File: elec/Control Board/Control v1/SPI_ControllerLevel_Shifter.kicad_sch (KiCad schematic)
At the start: 34 parts, among them J301 RJ12_6P6C_HORZ, J302 0.100_2Pin, Q301 BSS138, Q302 BSS138, Q303 BSS138, Q304 BSS138

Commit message: Update parts in schematic for BOM generation.
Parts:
- R308, R313, R316, R317: MPN RMC 0603 10K F N -> RMC060310KFN
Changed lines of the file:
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@@
       (effects (font (size 1.27 1.27)) hide)
     )
-    (property "Description" "100mW ±1% 1kΩ 0603 Chip Resistor" (at 120.65 83.82 0)
+    (property "Description" "0.1W ±1% 1kΩ 0603 Chip Resistor - Surface Mount ROHS" (at 120.65 83.82 0)
       (effects (font (size 1.27 1.27)) hide)
     )
@@
       (effects (font (size 1.27 1.27)) hide)
     )
-    (property "Datasheet" "~" (at 143.51 138.43 0)
+    (property "Datasheet" "https://datasheet.lcsc.com/lcsc/1811101310_TyoHM-RMC06031K1-N_C269704.pdf" (at 143.51 138.43 0)
       (effects (font (size 1.27 1.27)) hide)
     )
@@
       (effects (font (size 1.27 1.27)) hide)
     )
-    (property "MPN" "RMC 0603 10K F N" (at 143.51 138.43 0)
+    (property "MPN" "RMC060310KFN" (at 143.51 138.43 0)
       (effects (font (size 1.27 1.27)) hide)
     )
@@
       (effects (font (size 1.27 1.27)) hide)
     )
-    (property "Datasheet" "~" (at 142.24 176.53 0)
+    (property "Datasheet" "https://datasheet.lcsc.com/lcsc/1811101310_TyoHM-RMC06031K1-N_C269704.pdf" (at 142.24 176.53 0)
       (effects (font (size 1.27 1.27)) hide)
     )
@@
       (effects (font (size 1.27 1.27)) hide)
     )
-    (property "MPN" "RMC 0603 10K F N" (at 142.24 176.53 0)
+    (property "MPN" "RMC060310KFN" (at 142.24 176.53 0)
       (effects (font (size 1.27 1.27)) hide)
     )
@@
       (effects (font (size 1.27 1.27)) hide)
     )
-    (property "Datasheet" "~" (at 143.51 101.6 0)
+    (property "Datasheet" "https://datasheet.lcsc.com/lcsc/1811101310_TyoHM-RMC06031K1-N_C269704.pdf" (at 143.51 101.6 0)
       (effects (font (size 1.27 1.27)) hide)
     )
@@
       (effects (font (size 1.27 1.27)) hide)
     )
-    (property "MPN" "RMC 0603 10K F N" (at 143.51 101.6 0)
+    (property "MPN" "RMC060310KFN" (at 143.51 101.6 0)
       (effects (font (size 1.27 1.27)) hide)
     )
@@
       (effects (font (size 1.27 1.27)) hide)
     )
-    (property "Description" "100mW ±1% 1kΩ 0603 Chip Resistor" (at 119.38 158.75 0)
+    (property "Description" "0.1W ±1% 1kΩ 0603 Chip Resistor - Surface Mount ROHS" (at 119.38 158.75 0)
       (effects (font (size 1.27 1.27)) hide)
     )
@@
       (effects (font (size 1.27 1.27)) hide)
     )
-    (property "Datasheet" "~" (at 120.65 49.53 0)
+    (property "Datasheet" "https://datasheet.lcsc.com/lcsc/1811101310_TyoHM-RMC06031K1-N_C269704.pdf" (at 120.65 49.53 0)
       (effects (font (size 1.27 1.27)) hide)
     )
@@
       (effects (font (size 1.27 1.27)) hide)
     )
-    (property "MPN" "RMC 0603 10K F N" (at 120.65 49.53 0)
+    (property "MPN" "RMC060310KFN" (at 120.65 49.53 0)
       (effects (font (size 1.27 1.27)) hide)
     )
@@
       (effects (font (size 1.27 1.27)) hide)
     )
-    (property "Description" "100mW ±1% 1kΩ 0603 Chip Resistor" (at 120.65 120.65 0)
+    (property "Description" "0.1W ±1% 1kΩ 0603 Chip Resistor - Surface Mount ROHS" (at 120.65 120.65 0)
       (effects (font (size 1.27 1.27)) hide)
     )
@@
       (effects (font (size 1.27 1.27)) hide)
     )
-    (property "Description" "100mW ±1% 1kΩ 0603 Chip Resistor" (at 143.51 67.31 0)
-      (effects (font (size 1.27 1.27)) hide)
-    )
+    (property "Description" "0.1W ±1% 1kΩ 0603 Chip Resistor - Surface Mount ROHS" (at 143.51 67.31 0)
+      (effects (font (size 1.27 1.27)) hide)
+    )

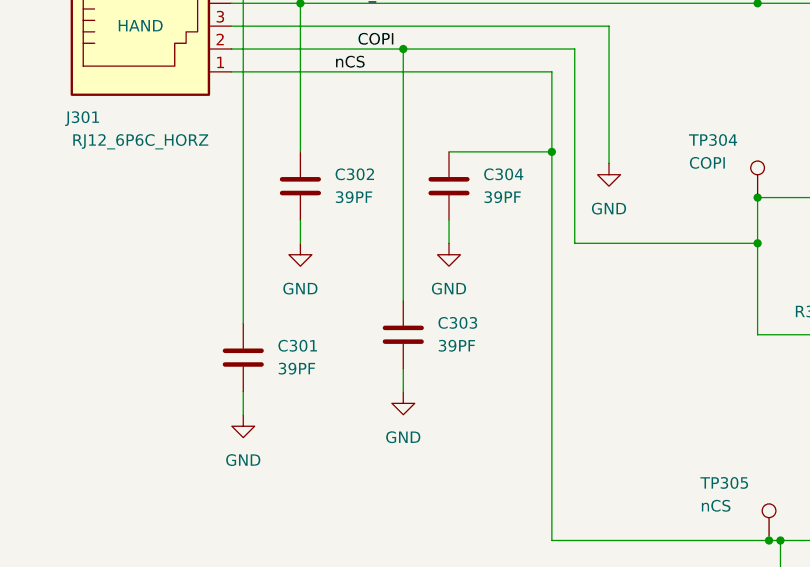
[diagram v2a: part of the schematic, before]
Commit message: Add BOM spread sheet and a JLCPCB BOM.
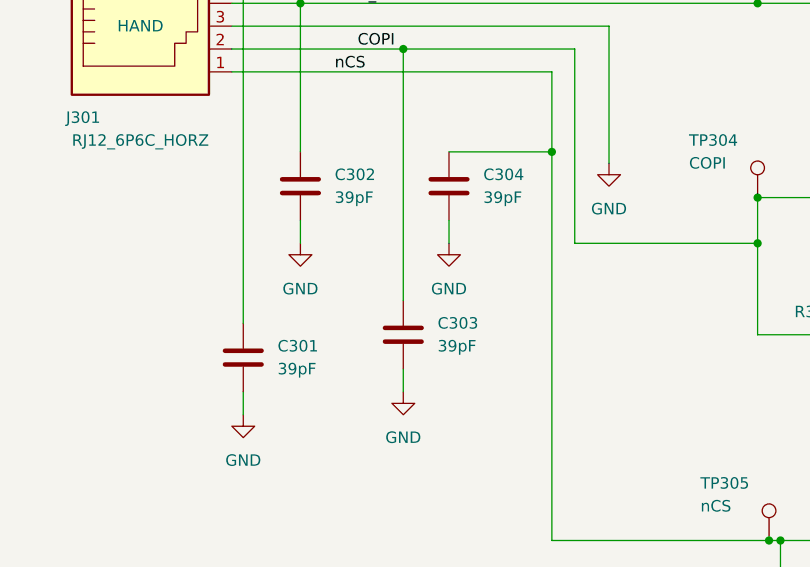
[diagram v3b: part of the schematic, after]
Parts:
- C301, C302, C303, C304: value 39PF -> 39pF; Cost 0.0025 -> 0.003
- C305, C306: Cost 0.0025 -> 0.0037; Distributor 1 PN (none) -> C91183; MPN (none) -> CC0603JRX7R9BB104
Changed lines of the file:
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@@
       (effects (font (size 1.27 1.27)) hide)
     )
-    (property "Datasheet" "https://datasheet.lcsc.com/lcsc/1811082118_YAGEO-CC0603JRNPO9BN390_C107049.pdf" (at 161.29 40.64 0)
+    (property "Datasheet" "CC0603JRX7R9BB104.pdf" (at 161.29 40.64 0)
       (effects (font (size 1.27 1.27)) hide)
     )
@@
       (effects (font (size 1.27 1.27)) hide)
     )
-    (property "Distributor 1 PN" "" (at 161.29 40.64 0)
-      (effects (font (size 1.27 1.27)) hide)
-    )
-    (property "Cost" "0.0025" (at 161.29 40.64 0)
-      (effects (font (size 1.27 1.27)) hide)
-    )
-    (property "MPN" "" (at 161.29 40.64 0)
+    (property "Distributor 1 PN" "C91183" (at 161.29 40.64 0)
+      (effects (font (size 1.27 1.27)) hide)
+    )
+    (property "Cost" "0.0037" (at 161.29 40.64 0)
+      (effects (font (size 1.27 1.27)) hide)
+    )
+    (property "MPN" "CC0603JRX7R9BB104" (at 161.29 40.64 0)
       (effects (font (size 1.27 1.27)) hide)
     )
@@
       (effects (font (size 1.27 1.27)) hide)
     )
-    (property "Datasheet" "https://datasheet.lcsc.com/lcsc/1811082118_YAGEO-CC0603JRNPO9BN390_C107049.pdf" (at 147.32 40.64 0)
+    (property "Datasheet" "CC0603JRX7R9BB104.pdf" (at 147.32 40.64 0)
       (effects (font (size 1.27 1.27)) hide)
     )
@@
       (effects (font (size 1.27 1.27)) hide)
     )
-    (property "Distributor 1 PN" "" (at 147.32 40.64 0)
-      (effects (font (size 1.27 1.27)) hide)
-    )
-    (property "Cost" "0.0025" (at 147.32 40.64 0)
-      (effects (font (size 1.27 1.27)) hide)
-    )
-    (property "MPN" "" (at 147.32 40.64 0)
+    (property "Distributor 1 PN" "C91183" (at 147.32 40.64 0)
+      (effects (font (size 1.27 1.27)) hide)
+    )
+    (property "Cost" "0.0037" (at 147.32 40.64 0)
+      (effects (font (size 1.27 1.27)) hide)
+    )
+    (property "MPN" "CC0603JRX7R9BB104" (at 147.32 40.64 0)
       (effects (font (size 1.27 1.27)) hide)
     )
@@
       (effects (font (size 1.27 1.27)) (justify left))
     )
-    (property "Value" "39PF" (at 78.74 126.9999 0)
+    (property "Value" "39pF" (at 78.74 126.9999 0)
       (effects (font (size 1.27 1.27)) (justify left))
     )
@@
       (effects (font (size 1.27 1.27)) hide)
     )
-    (property "Cost" "0.0025" (at 74.93 125.73 0)
+    (property "Cost" "0.003" (at 74.93 125.73 0)
       (effects (font (size 1.27 1.27)) hide)
     )
@@
       (effects (font (size 1.27 1.27)) (justify left))
     )
-    (property "Value" "39PF" (at 73.66 143.5099 0)
+    (property "Value" "39pF" (at 73.66 143.5099 0)
       (effects (font (size 1.27 1.27)) (justify left))
     )
@@
       (effects (font (size 1.27 1.27)) hide)
     )
-    (property "Cost" "0.0025" (at 69.85 142.24 0)
+    (property "Cost" "0.003" (at 69.85 142.24 0)
       (effects (font (size 1.27 1.27)) hide)
     )
@@
       (effects (font (size 1.27 1.27)) (justify left))
     )
-    (property "Value" "39PF" (at 55.88 146.0499 0)
+    (property "Value" "39pF" (at 55.88 146.0499 0)
       (effects (font (size 1.27 1.27)) (justify left))
     )
@@
       (effects (font (size 1.27 1.27)) hide)
     )
-    (property "Cost" "0.0025" (at 52.07 144.78 0)
+    (property "Cost" "0.003" (at 52.07 144.78 0)
       (effects (font (size 1.27 1.27)) hide)
     )
@@
       (effects (font (size 1.27 1.27)) (justify left))
     )
-    (property "Value" "39PF" (at 62.23 126.9999 0)
+    (property "Value" "39pF" (at 62.23 126.9999 0)
       (effects (font (size 1.27 1.27)) (justify left))
     )
@@
       (effects (font (size 1.27 1.27)) hide)
     )
-    (property "Cost" "0.0025" (at 58.42 125.73 0)
-      (effects (font (size 1.27 1.27)) hide)
-    )
+    (property "Cost" "0.003" (at 58.42 125.73 0)
+      (effects (font (size 1.27 1.27)) hide)
+    )
